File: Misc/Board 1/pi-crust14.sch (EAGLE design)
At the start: 46 parts, among them IC10 40193N, IC2 74LS595D, IC3 74LS595D, IC4 74LS595D, IC5 74LS595D, IC6 74LS595D, IC7 74LS595D, IC8 74AC11008, U1 AD9983AKSTZ_140, U2 SN54LS253_J_16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

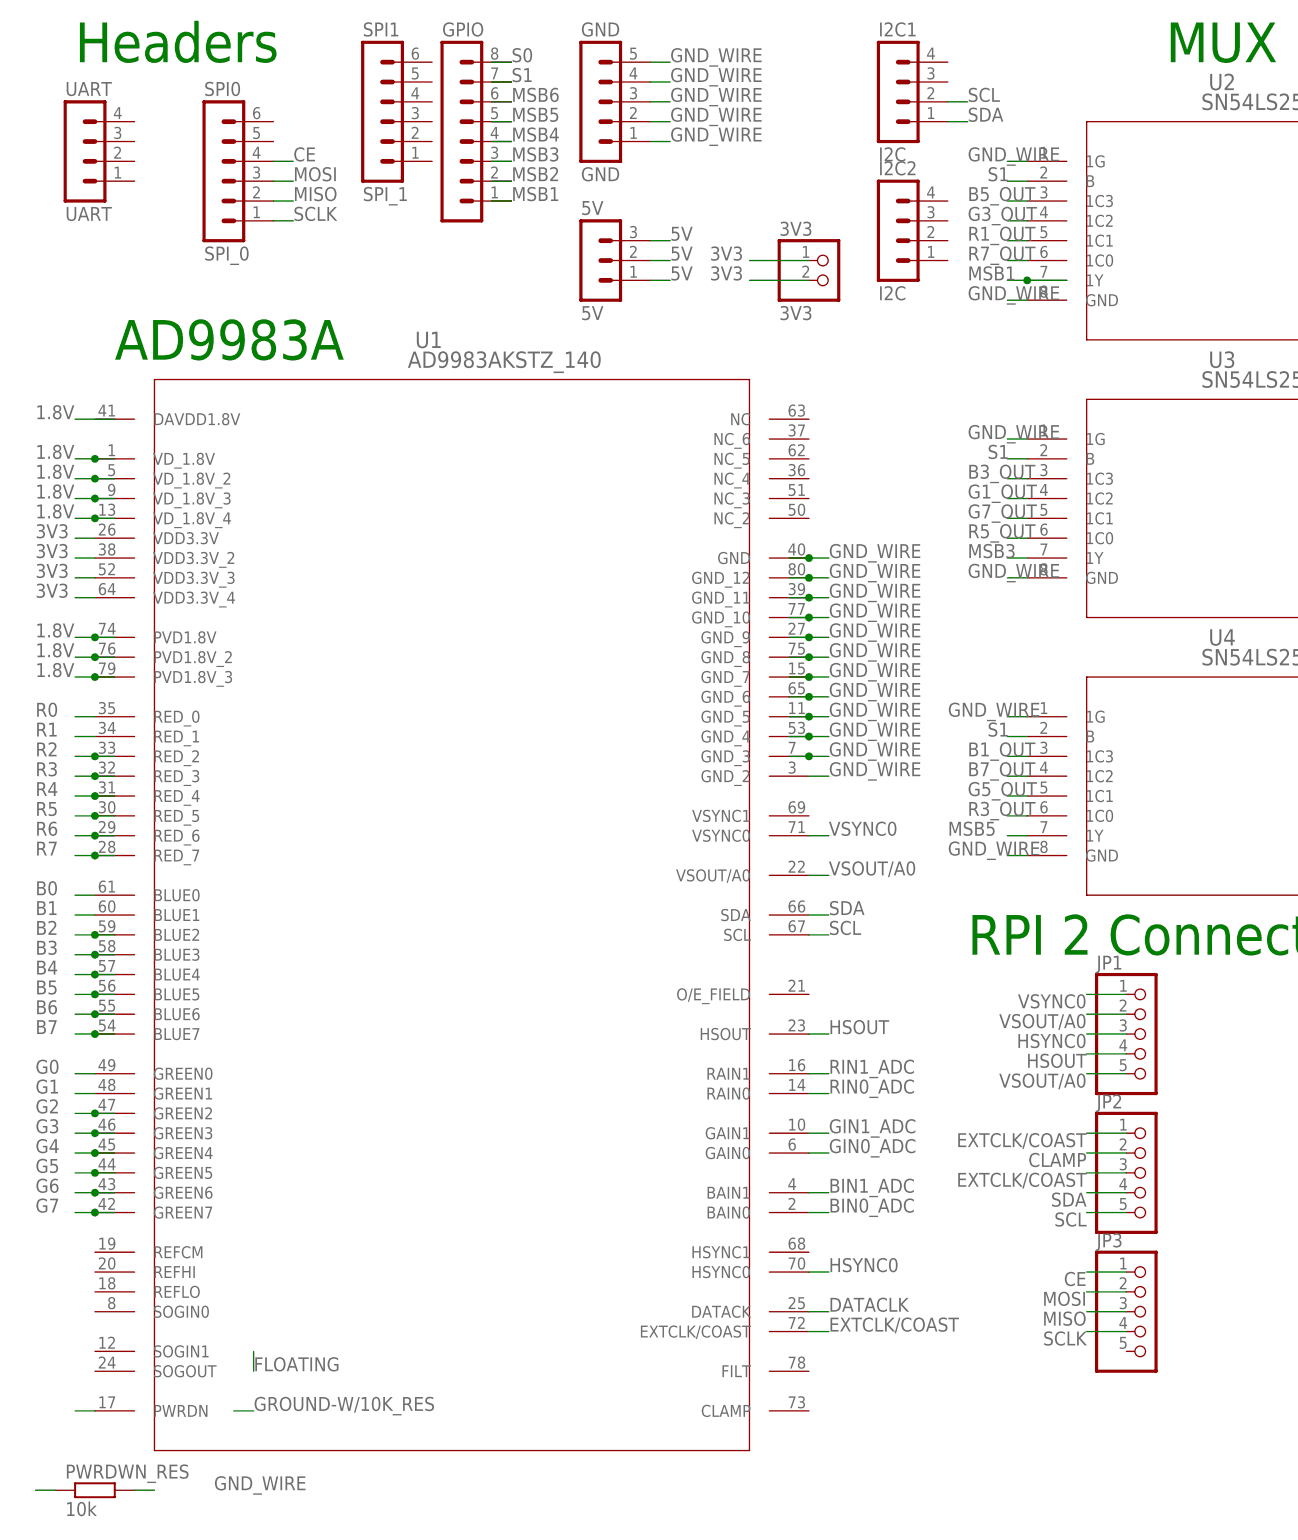
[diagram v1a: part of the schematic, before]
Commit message: Board Update 5
RCA and Filter still incorrect, all other functions verified and correct
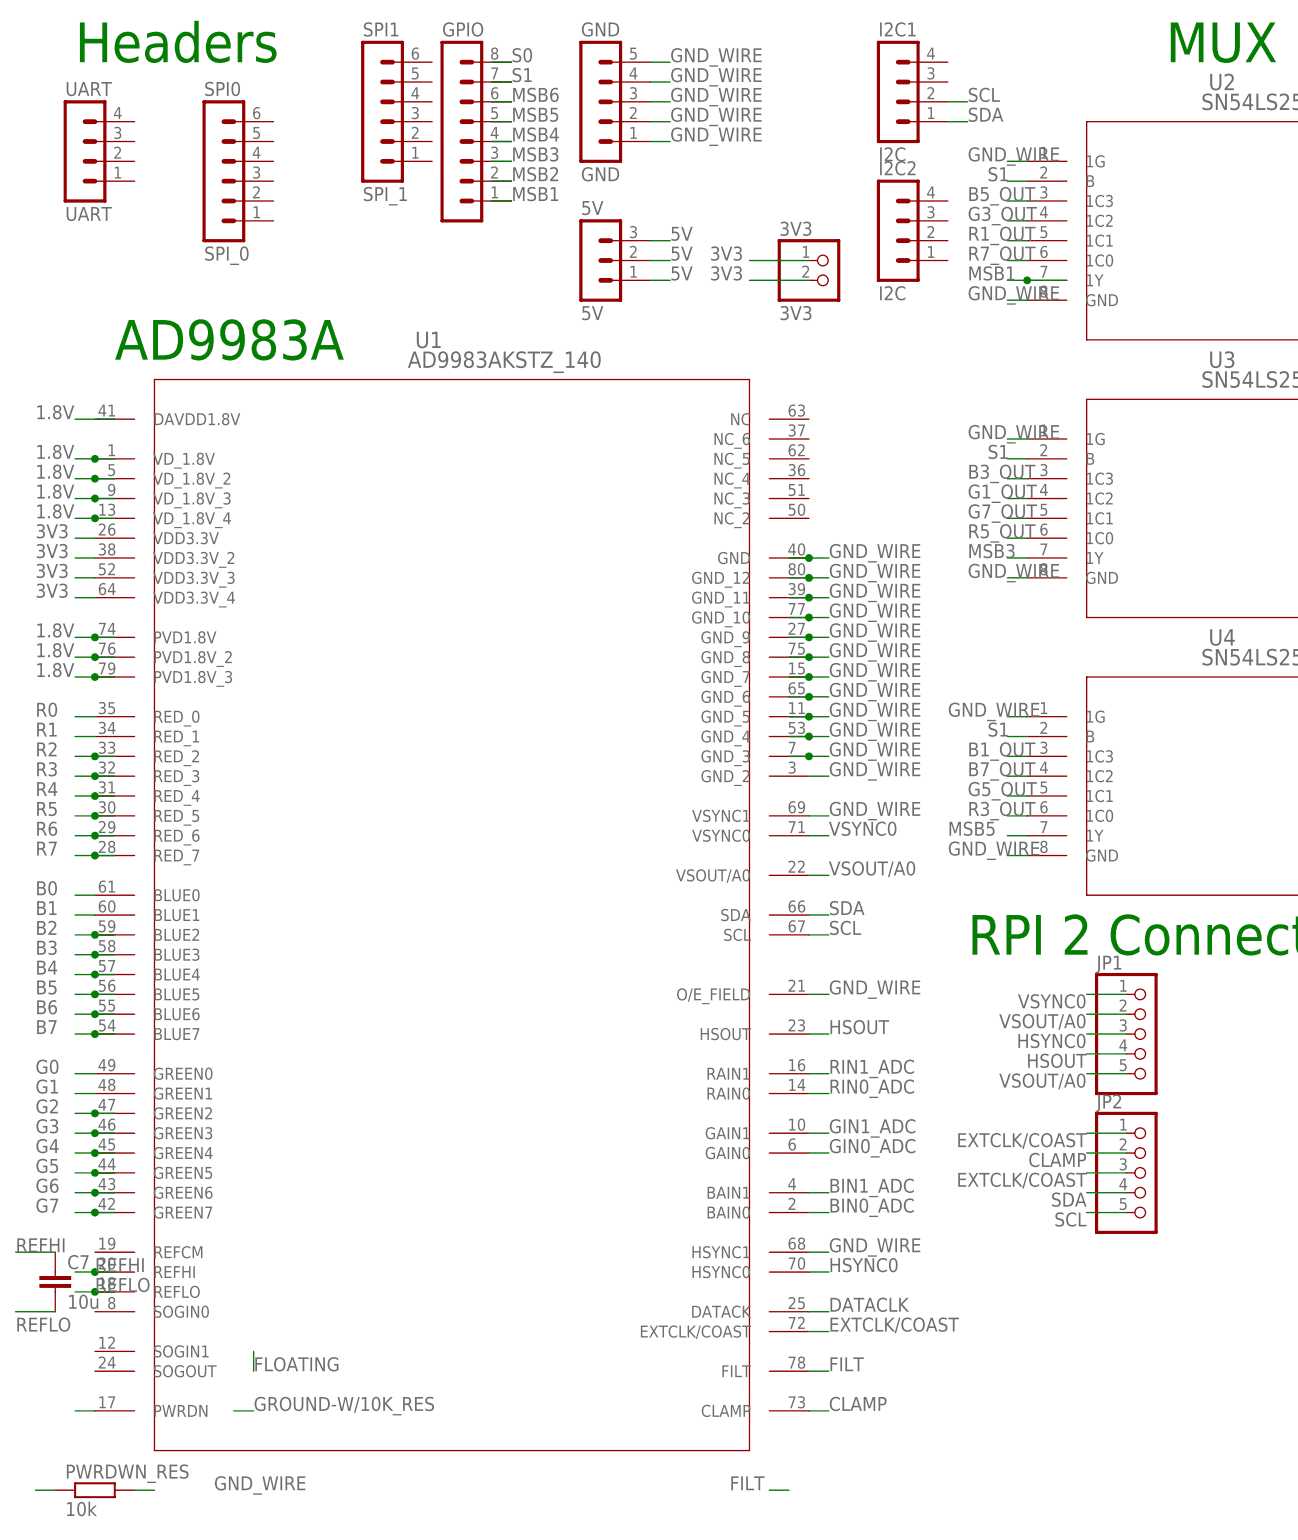
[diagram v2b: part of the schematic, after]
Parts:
- removed JP3: (no value), pinhead:PINHD-1X5
- added C7: 10u, capacitor-wima:C2.5/5
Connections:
- removed net CE: JP3.1, SPI0.4
- removed net MISO: JP3.3, SPI0.2
- removed net MOSI: JP3.2, SPI0.3
- removed net SCLK: JP3.4, SPI0.1
- new net FILT: U1.FILT
- new net REFHI: C7.1, U1.REFHI
- new net REFLO: C7.2, U1.REFLO
- net CLAMP: now also U1.CLAMP
- net GND_WIRE: now also U1.HSYNC1, U1.O/E_FIELD, U1.VSYNC1
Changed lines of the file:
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@@
 <part name="JP1" library="pinhead" deviceset="PINHD-1X5" device=""/>
 <part name="JP2" library="pinhead" deviceset="PINHD-1X5" device=""/>
-<part name="JP3" library="pinhead" deviceset="PINHD-1X5" device=""/>
+<part name="C7" library="capacitor-wima" deviceset="C" device="2.5/5" value="10u"/>
 </parts>
 <sheets>
@@
 <instance part="JP1" gate="A" x="142.24" y="53.34"/>
 <instance part="JP2" gate="A" x="142.24" y="35.56"/>
-<instance part="JP3" gate="A" x="142.24" y="17.78"/>
+<instance part="C7" gate="G$1" x="2.54" y="22.86"/>
 </instances>
 <busses>
@@
 <pinref part=".1UF" gate="G$1" pin="2"/>
 </segment>
+<segment>
+<wire x1="99.06" y1="81.28" x2="101.6" y2="81.28" width="0.8128" layer="91"/>
+<label x="101.6" y="81.28" size="1.778" layer="95"/>
+<pinref part="U1" gate="A" pin="VSYNC1"/>
+</segment>
+<segment>
+<wire x1="99.06" y1="58.42" x2="101.6" y2="58.42" width="0.8128" layer="91"/>
+<label x="101.6" y="58.42" size="1.778" layer="95"/>
+<pinref part="U1" gate="A" pin="O/E_FIELD"/>
+</segment>
+<segment>
+<wire x1="99.06" y1="25.4" x2="101.6" y2="25.4" width="0.8128" layer="91"/>
+<label x="101.6" y="25.4" size="1.778" layer="95"/>
+<pinref part="U1" gate="A" pin="HSYNC1"/>
+</segment>
 </net>
 <net name="S0" class="0">
@@
 </segment>
 </net>
-<net name="SCLK" class="0">
-<segment>
-<pinref part="SPI0" gate="1" pin="1"/>
-<wire x1="30.48" y1="157.48" x2="33.02" y2="157.48" width="0.3048" layer="91"/>
-<label x="33.02" y="157.48" size="1.778" layer="95"/>
-</segment>
-<segment>
-<wire x1="134.62" y1="15.24" x2="139.7" y2="15.24" width="0.3048" layer="91"/>
-<label x="134.62" y="15.24" size="1.778" layer="95" rot="R180"/>
-<pinref part="JP3" gate="A" pin="4"/>
-</segment>
-</net>
-<net name="MISO" class="0">
-<segment>
-<pinref part="SPI0" gate="1" pin="2"/>
-<wire x1="30.48" y1="160.02" x2="33.02" y2="160.02" width="0.3048" layer="91"/>
-<label x="33.02" y="160.02" size="1.778" layer="95"/>
-</segment>
-<segment>
-<wire x1="134.62" y1="17.78" x2="139.7" y2="17.78" width="0.3048" layer="91"/>
-<label x="134.62" y="17.78" size="1.778" layer="95" rot="R180"/>
-<pinref part="JP3" gate="A" pin="3"/>
-</segment>
-</net>
-<net name="MOSI" class="0">
-<segment>
-<pinref part="SPI0" gate="1" pin="3"/>
-<wire x1="30.48" y1="162.56" x2="33.02" y2="162.56" width="0.3048" layer="91"/>
-<label x="33.02" y="162.56" size="1.778" layer="95"/>
-</segment>
-<segment>
-<wire x1="134.62" y1="20.32" x2="139.7" y2="20.32" width="0.3048" layer="91"/>
-<label x="134.62" y="20.32" size="1.778" layer="95" rot="R180"/>
-<pinref part="JP3" gate="A" pin="2"/>
-</segment>
-</net>
-<net name="CE" class="0">
-<segment>
-<pinref part="SPI0" gate="1" pin="4"/>
-<wire x1="30.48" y1="165.1" x2="33.02" y2="165.1" width="0.3048" layer="91"/>
-<label x="33.02" y="165.1" size="1.778" layer="95"/>
-</segment>
-<segment>
-<wire x1="134.62" y1="22.86" x2="139.7" y2="22.86" width="0.3048" layer="91"/>
-<label x="134.62" y="22.86" size="1.778" layer="95" rot="R180"/>
-<pinref part="JP3" gate="A" pin="1"/>
-</segment>
-</net>
 <net name="VSYNC0" class="0">
 <segment>
@@
 <label x="134.62" y="38.1" size="1.778" layer="95" rot="R180"/>
 </segment>
-</net>
+<segment>
+<wire x1="101.6" y1="5.08" x2="99.06" y2="5.08" width="0.3048" layer="91"/>
+<label x="101.6" y="5.08" size="1.778" layer="95"/>
+<pinref part="U1" gate="A" pin="CLAMP"/>
+</segment>
+</net>
+<net name="REFHI" class="0">
+<segment>
+<pinref part="C7" gate="G$1" pin="1"/>
+<wire x1="2.54" y1="25.4" x2="-2.54" y2="25.4" width="0.3048" layer="91"/>
+<label x="-2.54" y="25.4" size="1.778" layer="95"/>
+</segment>
+<segment>
+<wire x1="10.16" y1="22.86" x2="7.62" y2="22.86" width="0.3048" layer="91"/>
+<label x="7.62" y="22.86" size="1.778" layer="95"/>
+<pinref part="U1" gate="A" pin="REFHI"/>
+<wire x1="7.62" y1="22.86" x2="5.08" y2="22.86" width="0.3048" layer="91"/>
+<junction x="7.62" y="22.86"/>
+</segment>
+</net>
+<net name="REFLO" class="0">
+<segment>
+<pinref part="C7" gate="G$1" pin="2"/>
+<wire x1="2.54" y1="17.78" x2="-2.54" y2="17.78" width="0.3048" layer="91"/>
+<label x="-2.54" y="15.24" size="1.778" layer="95"/>
+</segment>
+<segment>
+<wire x1="10.16" y1="20.32" x2="7.62" y2="20.32" width="0.3048" layer="91"/>
+<label x="7.62" y="20.32" size="1.778" layer="95"/>
+<pinref part="U1" gate="A" pin="REFLO"/>
+<wire x1="7.62" y1="20.32" x2="5.08" y2="20.32" width="0.3048" layer="91"/>
+<junction x="7.62" y="20.32"/>
+</segment>
+</net>
+<net name="FILT" class="0">
+<segment>
+<pinref part="U1" gate="A" pin="FILT"/>
+<wire x1="99.06" y1="10.16" x2="101.6" y2="10.16" width="0.3048" layer="91"/>
+<label x="101.6" y="10.16" size="1.778" layer="95"/>
+</segment>
+<segment>
+<wire x1="93.98" y1="-5.08" x2="96.52" y2="-5.08" width="0.3048" layer="91"/>
+<label x="88.9" y="-5.08" size="1.778" layer="95"/>
+</segment>
+</net>

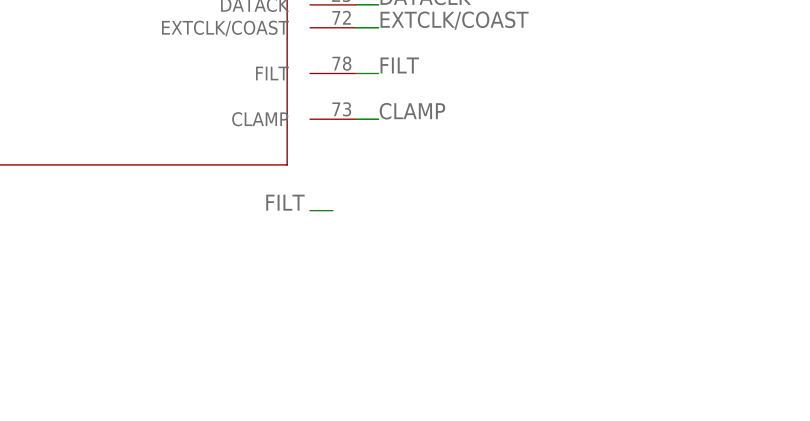
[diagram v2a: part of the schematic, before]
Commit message: Board Update 6
RCA and wire size still incorrect (everything else complete), Filter
added, ADC correct, Removal of unnecessary wires
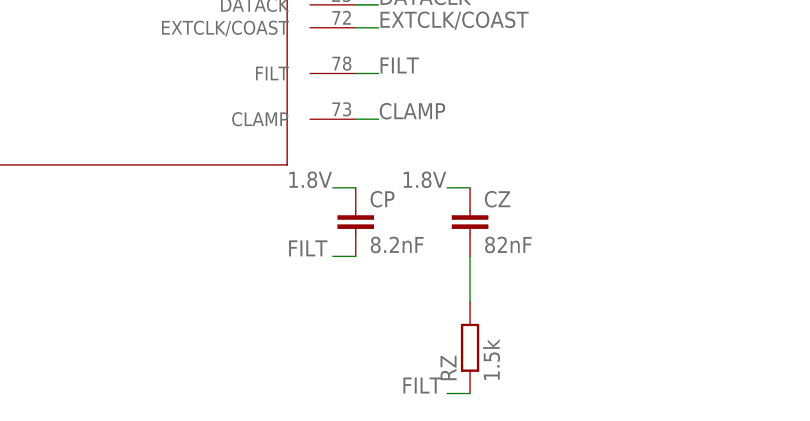
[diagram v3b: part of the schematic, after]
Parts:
- added CP: 8.2nF, capacitor-wima:C2.5/5
- added CZ: 82nF, capacitor-wima:C2.5/5
- added RZ: 1.5k, eagle-ltspice:R0204/7
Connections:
- new net N$1: CZ.2, RZ.2
- net 1.8V: now also CP.1, CZ.1
- net FILT: now also CP.2, RZ.1
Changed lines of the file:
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@@
 <part name="JP2" library="pinhead" deviceset="PINHD-1X5" device=""/>
 <part name="C7" library="capacitor-wima" deviceset="C" device="2.5/5" value="10u"/>
+<part name="CZ" library="capacitor-wima" deviceset="C" device="2.5/5" value="82nF"/>
+<part name="CP" library="capacitor-wima" deviceset="C" device="2.5/5" value="8.2nF"/>
+<part name="RZ" library="eagle-ltspice" deviceset="R" device="0204/7" value="1.5k"/>
 </parts>
 <sheets>
@@
 <instance part="JP2" gate="A" x="142.24" y="35.56"/>
 <instance part="C7" gate="G$1" x="2.54" y="22.86"/>
+<instance part="CZ" gate="G$1" x="111.76" y="-5.08"/>
+<instance part="CP" gate="G$1" x="99.06" y="-5.08"/>
+<instance part="RZ" gate="G$1" x="111.76" y="-20.32" rot="R90"/>
 </instances>
 <busses>
@@
 <pinref part=".1UF" gate="G$1" pin="1"/>
 </segment>
+<segment>
+<wire x1="96.52" y1="-2.54" x2="99.06" y2="-2.54" width="0.6096" layer="91"/>
+<label x="91.44" y="-2.54" size="1.778" layer="95"/>
+<pinref part="CP" gate="G$1" pin="1"/>
+</segment>
+<segment>
+<wire x1="109.22" y1="-2.54" x2="111.76" y2="-2.54" width="0.6096" layer="91"/>
+<label x="104.14" y="-2.54" size="1.778" layer="95"/>
+<pinref part="CZ" gate="G$1" pin="1"/>
+</segment>
 </net>
 <net name="FLOATING" class="0">
@@
 </segment>
 <segment>
-<wire x1="93.98" y1="-5.08" x2="96.52" y2="-5.08" width="0.3048" layer="91"/>
-<label x="88.9" y="-5.08" size="1.778" layer="95"/>
-</segment>
-</net>
+<wire x1="96.52" y1="-10.16" x2="99.06" y2="-10.16" width="0.3048" layer="91"/>
+<label x="91.44" y="-10.16" size="1.778" layer="95"/>
+<pinref part="CP" gate="G$1" pin="2"/>
+</segment>
+<segment>
+<wire x1="109.22" y1="-25.4" x2="111.76" y2="-25.4" width="0.3048" layer="91"/>
+<label x="104.14" y="-25.4" size="1.778" layer="95"/>
+<pinref part="RZ" gate="G$1" pin="1"/>
+</segment>
+</net>
+<net name="N$1" class="0">
+<segment>
+<pinref part="RZ" gate="G$1" pin="2"/>
+<pinref part="CZ" gate="G$1" pin="2"/>
+<wire x1="111.76" y1="-15.24" x2="111.76" y2="-10.16" width="0.1524" layer="91"/>
+</segment>
+</net>
